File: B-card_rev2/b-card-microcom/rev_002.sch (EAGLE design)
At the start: 53 parts, among them IC1 AZ1117IH-5.0, IC2 AZ1117IH-5.0, IC3 AZ1117IH-5.0, IC4 DMN2041L-7, IC5 DMN2041L-7, IC6 DMN2041L-7, IC7 AZ1117IH-3.3, J1 10118192-0002LF, SW1 B3AL-1000P, U1 ATMEGA32U4-MU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

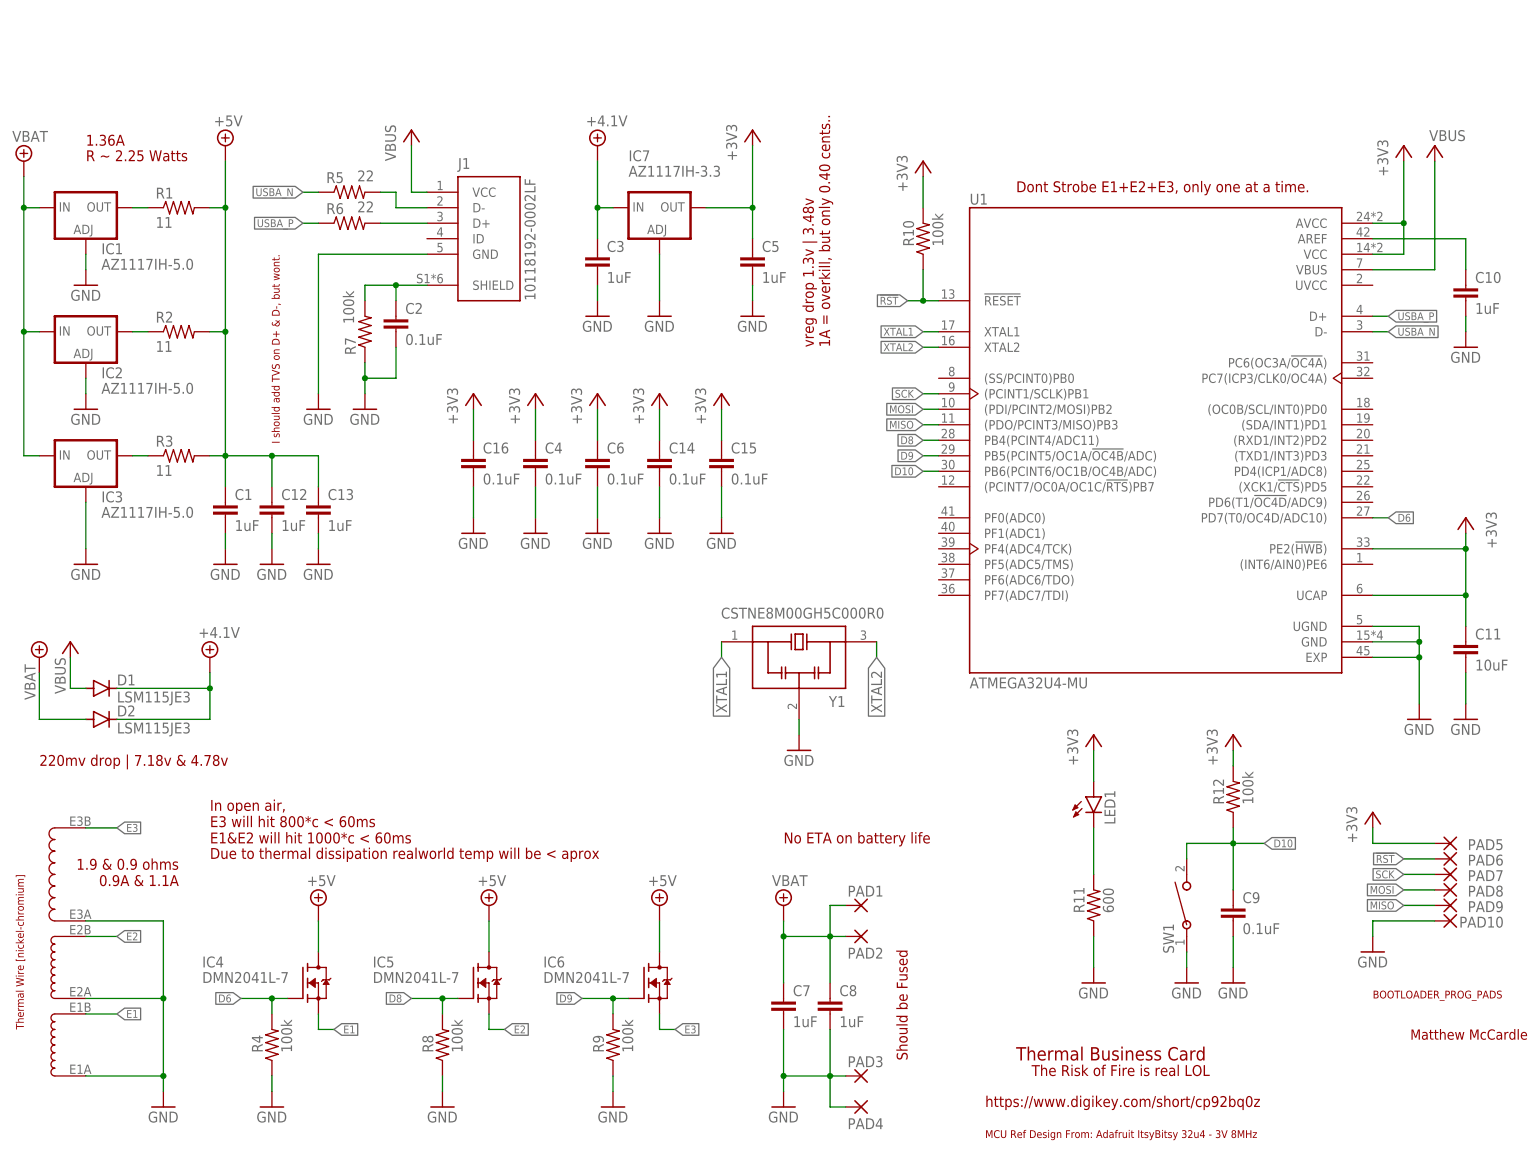
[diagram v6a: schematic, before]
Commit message: not rev-ed
Changed the sch and board, adapted for higher current.
Made small change to sketch, removed thermal approx.
exported new Gerber's.
changed BOM to reflect new design.

layout change now ready for fab, still needs a once over to correct any mistakes that I may have missed.
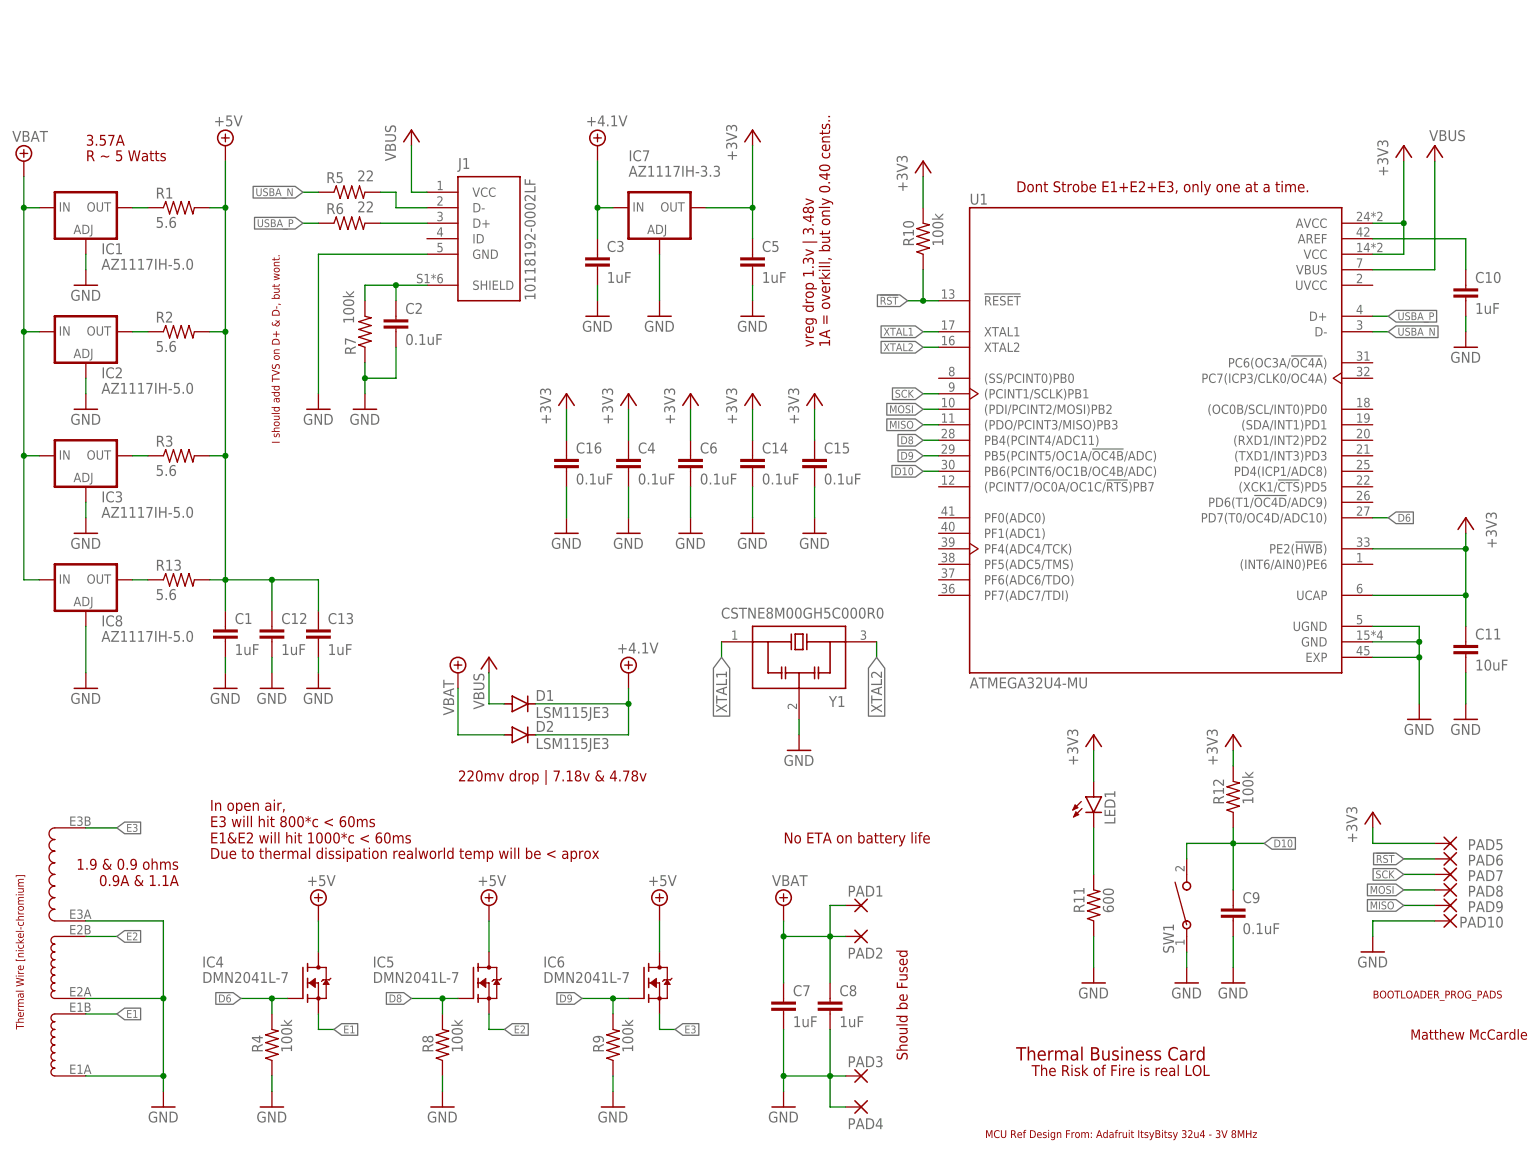
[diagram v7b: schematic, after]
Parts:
- added IC8: AZ1117IH-5.0, v-reg-edit:AZ1117IH
- added R13: 5.6, rcl:R-US_R2512
- R1, R2, R3: value 11 -> 5.6
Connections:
- new net N$1: IC8.OUT, R13.1
- net +5V: now also R13.2
- net +8V: now also IC8.IN
- net GND: now also IC8.ADJ
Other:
- note added: "3.57A"
- note added: "R ~ 5 Watts"
- note removed: "1.36A"
- note removed: "R ~ 2.25 Watts"
- note removed: "https://www.digikey.com/short/cp92bq0z"
- moved on the sheet: C1, C12, C13, C14, C15, C16, C4, C6, D1, D2
